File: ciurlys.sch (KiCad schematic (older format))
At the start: 20 parts, among them IC1 ATTINY9-TS, P1 CONN_01X02, P2 TPI, P3 OUTPUT, P4 INPUT, Q1 Q_NMOS_GSD

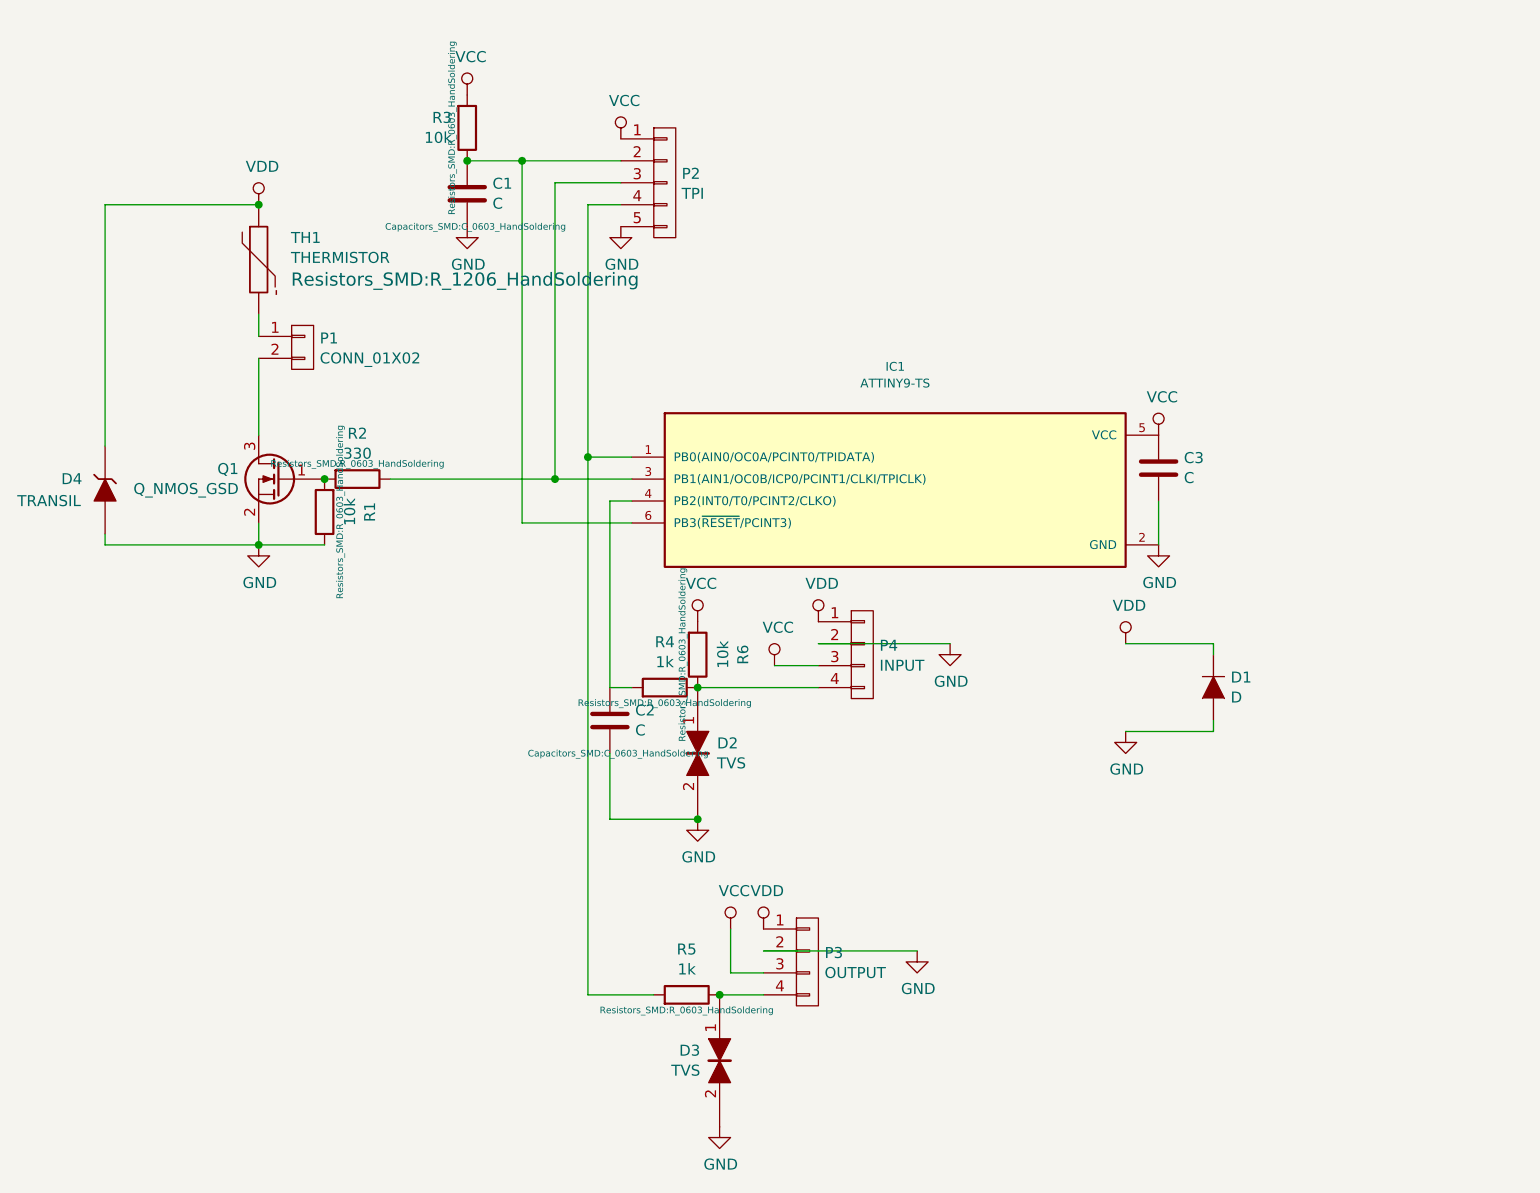
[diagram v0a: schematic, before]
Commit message: Make schematics nicer, add zeners on vdd and vcc
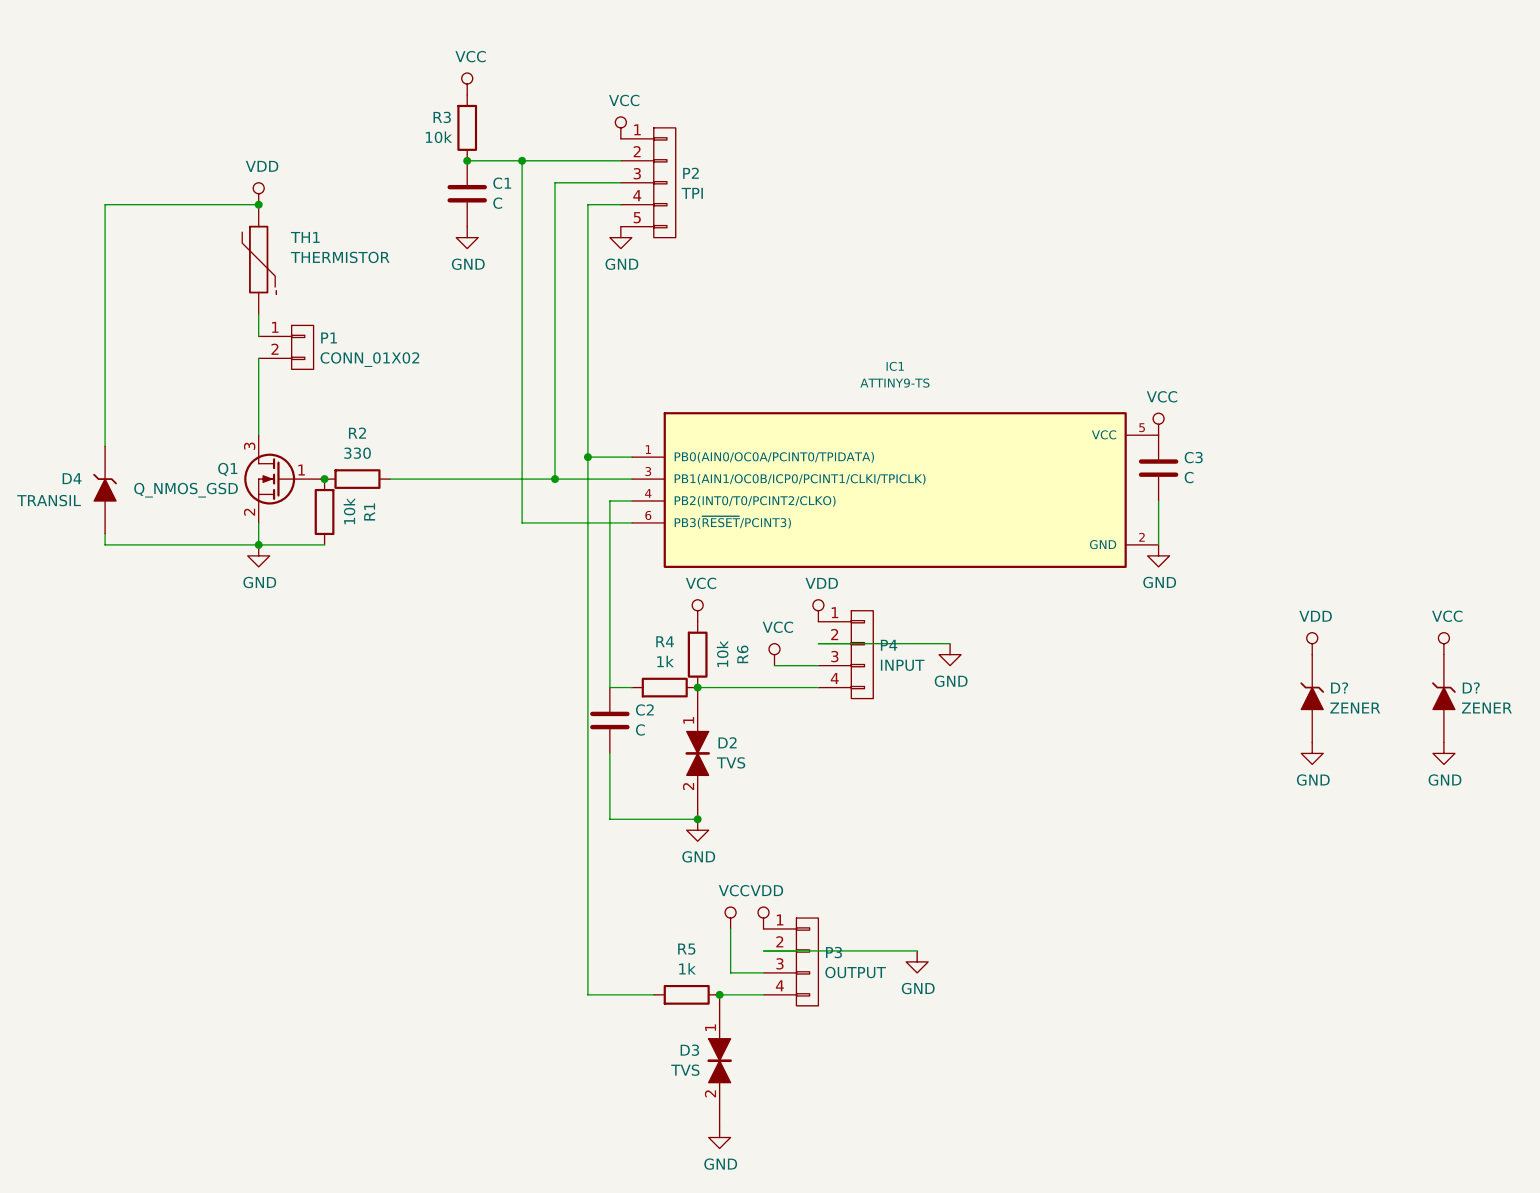
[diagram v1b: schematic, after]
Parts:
- removed D1: D, symbol D
- added D? (x2): ZENER, symbol ZENER
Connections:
- net GND: now also D?.1 (A), D?.1 (A)
- net VCC: now also D?.2 (K)
- net VDD: now also D?.2 (K)
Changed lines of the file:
@@
 F 0 "R3" H 5881 3104 50  0000 R CNN
 F 1 "10k" H 5881 3195 50  0000 R CNN
-F 2 "Resistors_SMD:R_0603_HandSoldering" V 5880 3150 30  0000 C CNN
+F 2 "Resistors_SMD:R_0603_HandSoldering" V 5880 3150 30  0001 C CNN
 F 3 "" H 5950 3150 30  0000 C CNN
 F 4 "?" H 5950 3150 60  0001 C CNN "PartNo"
@@
 F 0 "C1" H 6065 3496 50  0000 L CNN
 F 1 "C" H 6065 3405 50  0000 L CNN
-F 2 "Capacitors_SMD:C_0603_HandSoldering" H 5988 3300 30  0000 C CNN
+F 2 "Capacitors_SMD:C_0603_HandSoldering" H 5988 3300 30  0001 C CNN
 F 3 "" H 5950 3450 60  0000 C CNN
 F 4 "?" H 5950 3450 60  0001 C CNN "PartNo"
@@
 F 0 "R2" V 5243 4750 50  0000 C CNN
 F 1 "330" V 5334 4750 50  0000 C CNN
-F 2 "Resistors_SMD:R_0603_HandSoldering" V 5380 4750 30  0000 C CNN
+F 2 "Resistors_SMD:R_0603_HandSoldering" V 5380 4750 30  0001 C CNN
 F 3 "" H 5450 4750 30  0000 C CNN
 F 4 "?" H 5450 4750 60  0001 C CNN "PartNo"
@@
 F 0 "R4" V 7057 5700 50  0000 C CNN
 F 1 "1k" V 6966 5700 50  0000 C CNN
-F 2 "Resistors_SMD:R_0603_HandSoldering" V 6780 5700 30  0000 C CNN
+F 2 "Resistors_SMD:R_0603_HandSoldering" V 6780 5700 30  0001 C CNN
 F 3 "" H 6850 5700 30  0000 C CNN
 F 4 "?" H 6850 5700 60  0001 C CNN "PartNo"
@@
 	1    0    0    -1
 $EndComp
-$Comp
-L D D1
-U 1 1 57B56681
-P 9350 5700
-F 0 "D1" V 9396 5622 50  0000 R CNN
-F 1 "D" V 9305 5622 50  0000 R CNN
-F 2 "" H 9350 5700 60  0000 C CNN
-F 3 "" H 9350 5700 60  0000 C CNN
-	1    9350 5700
-	0    -1   -1   0
-$EndComp
 Wire Wire Line
 	5600 4750 6700 4750
@@
 F 0 "R5" V 7157 7100 50  0000 C CNN
 F 1 "1k" V 7066 7100 50  0000 C CNN
-F 2 "Resistors_SMD:R_0603_HandSoldering" V 6880 7100 30  0000 C CNN
+F 2 "Resistors_SMD:R_0603_HandSoldering" V 6880 7100 30  0001 C CNN
 F 3 "" H 6950 7100 30  0000 C CNN
 F 4 "?" H 6950 7100 60  0001 C CNN "PartNo"
@@
 F 0 "R6" V 7207 5550 50  0000 C CNN
 F 1 "10k" V 7116 5550 50  0000 C CNN
-F 2 "Resistors_SMD:R_0603_HandSoldering" V 6930 5550 30  0000 C CNN
+F 2 "Resistors_SMD:R_0603_HandSoldering" V 6930 5550 30  0001 C CNN
 F 3 "" H 7000 5550 30  0000 C CNN
 F 4 "?" H 7000 5550 60  0001 C CNN "PartNo"
@@
 F 0 "C2" H 6715 5896 50  0000 L CNN
 F 1 "C" H 6715 5805 50  0000 L CNN
-F 2 "Capacitors_SMD:C_0603_HandSoldering" H 6638 5700 30  0000 C CNN
+F 2 "Capacitors_SMD:C_0603_HandSoldering" H 6638 5700 30  0001 C CNN
 F 3 "" H 6600 5850 60  0000 C CNN
 F 4 "?" H 6600 5850 60  0001 C CNN "PartNo"
@@
 F 0 "R1" V 5093 4900 50  0000 C CNN
 F 1 "10k" V 5184 4900 50  0000 C CNN
-F 2 "Resistors_SMD:R_0603_HandSoldering" V 5230 4900 30  0000 C CNN
+F 2 "Resistors_SMD:R_0603_HandSoldering" V 5230 4900 30  0001 C CNN
 F 3 "" H 5300 4900 30  0000 C CNN
 F 4 "?" H 5300 4900 60  0001 C CNN "PartNo"
@@
 F 0 "TH1" H 5147 3849 50  0000 L CNN
 F 1 "THERMISTOR" H 5147 3758 50  0000 L CNN
-F 2 "Resistors_SMD:R_1206_HandSoldering" H 5147 3659 60  0000 L CNN
+F 2 "Resistors_SMD:R_1206_HandSoldering" H 5147 3659 60  0001 L CNN
 F 3 "" H 5000 3750 60  0000 C CNN
 F 4 "?" H 5000 3750 60  0001 C CNN "PartNo"
@@
 L VDD #PWR018
 U 1 1 57B6F356
-P 8950 5500
-F 0 "#PWR018" H 8950 5350 50  0001 C CNN
-F 1 "VDD" H 8967 5673 50  0000 C CNN
-F 2 "" H 8950 5500 60  0000 C CNN
-F 3 "" H 8950 5500 60  0000 C CNN
-	1    8950 5500
+P 9800 5550
+F 0 "#PWR018" H 9800 5400 50  0001 C CNN
+F 1 "VDD" H 9817 5723 50  0000 C CNN
+F 2 "" H 9800 5550 60  0000 C CNN
+F 3 "" H 9800 5550 60  0000 C CNN
+	1    9800 5550
 	1    0    0    -1
 $EndComp
@@
 L GND #PWR019
 U 1 1 57B6F39D
-P 8950 5900
-F 0 "#PWR019" H 8950 5650 50  0001 C CNN
-F 1 "GND" H 8955 5727 50  0000 C CNN
-F 2 "" H 8950 5900 60  0000 C CNN
-F 3 "" H 8950 5900 60  0000 C CNN
-	1    8950 5900
-	1    0    0    -1
-$EndComp
-Wire Wire Line
-	8950 5900 9350 5900
-Wire Wire Line
-	9350 5900 9350 5850
-Wire Wire Line
-	9350 5550 9350 5500
-Wire Wire Line
-	9350 5500 8950 5500
+P 9800 5950
+F 0 "#PWR019" H 9800 5700 50  0001 C CNN
+F 1 "GND" H 9805 5777 50  0000 C CNN
+F 2 "" H 9800 5950 60  0000 C CNN
+F 3 "" H 9800 5950 60  0000 C CNN
+	1    9800 5950
+	1    0    0    -1
+$EndComp
 Wire Wire Line
 	4300 5050 5300 5050
@@
 	4300 3500 5000 3500
 Connection ~ 5000 3500
+$Comp
+L ZENER D?
+U 1 1 57CD8161
+P 9800 5750
+F 0 "D?" V 9846 5671 50  0000 R CNN
+F 1 "ZENER" V 9755 5671 50  0000 R CNN
+F 2 "" H 9800 5750 60  0000 C CNN
+F 3 "" H 9800 5750 60  0000 C CNN
+	1    9800 5750
+	0    -1   -1   0
+$EndComp
+$Comp
+L ZENER D?
+U 1 1 57CD8353
+P 10400 5750
+F 0 "D?" V 10446 5671 50  0000 R CNN
+F 1 "ZENER" V 10355 5671 50  0000 R CNN
+F 2 "" H 10400 5750 60  0000 C CNN
+F 3 "" H 10400 5750 60  0000 C CNN
+	1    10400 5750
+	0    -1   -1   0
+$EndComp
+$Comp
+L VCC #PWR?
+U 1 1 57CD83CB
+P 10400 5550
+F 0 "#PWR?" H 10400 5400 50  0001 C CNN
+F 1 "VCC" H 10417 5723 50  0000 C CNN
+F 2 "" H 10400 5550 60  0000 C CNN
+F 3 "" H 10400 5550 60  0000 C CNN
+	1    10400 5550
+	1    0    0    -1
+$EndComp
+$Comp
+L GND #PWR?
+U 1 1 57CD8415
+P 10400 5950
+F 0 "#PWR?" H 10400 5700 50  0001 C CNN
+F 1 "GND" H 10405 5777 50  0000 C CNN
+F 2 "" H 10400 5950 60  0000 C CNN
+F 3 "" H 10400 5950 60  0000 C CNN
+	1    10400 5950
+	1    0    0    -1
+$EndComp
 $EndSCHEMATC
